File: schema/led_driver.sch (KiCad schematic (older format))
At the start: 1 part

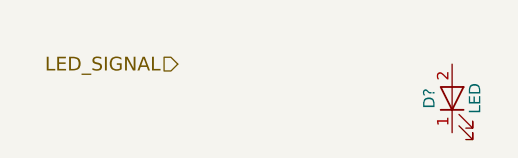
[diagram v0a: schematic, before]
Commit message: Preamp prototype, add IR LED and photodiode
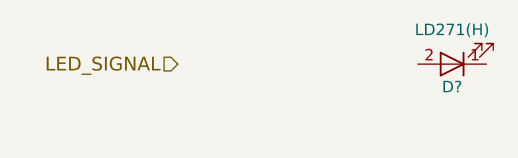
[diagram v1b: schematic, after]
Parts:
- D?: value LED -> LD271(H)
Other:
- moved on the sheet: D?
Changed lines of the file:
@@
 $Descr A4 11693 8268
 encoding utf-8
-Sheet 4 6
+Sheet 3 6
 Title ""
 Date ""
@@
 L LED D?
 U 1 1 5910407B
-P 4400 2350
-F 0 "D?" H 4400 2450 50  0000 C CNN
-F 1 "LED" H 4400 2250 50  0000 C CNN
-F 2 "" H 4400 2350 50  0000 C CNN
-F 3 "" H 4400 2350 50  0000 C CNN
-	1    4400 2350
-	0    -1   -1   0
+P 4400 2200
+F 0 "D?" H 4400 2300 50  0000 C CNN
+F 1 "LD271(H)" H 4400 2050 50  0000 C CNN
+F 2 "" H 4400 2200 50  0000 C CNN
+F 3 "" H 4400 2200 50  0000 C CNN
+	1    4400 2200
+	-1   0    0    1
 $EndComp
 $EndSCHEMATC
